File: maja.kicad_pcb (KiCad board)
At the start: 2 copper layers, 0 parts

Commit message: Started with basic PCB layout. Footprints must be checked again! I just choose one to be able to do a prelimary placement
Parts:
- added C1: 1uF, SMD_Packages:SM0603_Capa, F.Cu at (5.08, -5.08)
- added C10: 1uF, SMD_Packages:SM0603_Capa, F.Cu at (8.89, -6.35)
- added C11: 100nF, SMD_Packages:SM0603_Capa, F.Cu at (5.08, -2.54)
- added C12: 100nF, SMD_Packages:SM0603_Capa, F.Cu at (-8.89, -3.81)
- added C13: 1uF, SMD_Packages:SM0603_Capa, F.Cu at (1.27, -7.62)
- added C14: 100nF, SMD_Packages:SM0603_Capa, F.Cu at (-14.0, -1.27)
- added C15: 100nF, SMD_Packages:SM0603_Capa, F.Cu at (-10.2, -7.62)
- added C16: 100nF, SMD_Packages:SM0603_Capa, F.Cu at (-2.54, -5.08)
- added C17: 100nF, SMD_Packages:SM0603_Capa, F.Cu at (-8.89, -1.27)
- added C18: C, SMD_Packages:SM0603_Capa, F.Cu at (101.1, 99.8)
- added C19: C, SMD_Packages:SM0603_Capa, F.Cu at (90.2, 94.0)
- added C2: 1uF, SMD_Packages:SM0603_Capa, F.Cu at (6.35, 2.54)
- added C20: C, SMD_Packages:SM0603_Capa, F.Cu at (92.1, 94.0)
- added C21: 47p, SMD_Packages:SM0603_Capa, F.Cu at (0.00, -1.27)
- added C22: 1uF, SMD_Packages:SM0603_Capa, F.Cu at (119.4, 110.2)
- added C23: C, SMD_Packages:SM0603_Capa, F.Cu at (89.4, 90.9)
- added C24: C, SMD_Packages:SM0603_Capa, F.Cu at (91.9, 87.6)
- added C25: 2.2uF, SMD_Packages:SM0603_Capa, F.Cu at (108.7, 114.0)
- added C26: C, SMD_Packages:SM0603_Capa, F.Cu at (91.7, 80.5)
- added C27: C, SMD_Packages:SM0603_Capa, F.Cu at (83.8, 128.0)
- added C28: C, SMD_Packages:SM0603_Capa, F.Cu at (91.9, 140.2)
- added C3: 12pF, SMD_Packages:SM0603_Capa, F.Cu at (102.4, 87.9)
- added C31: 47p, SMD_Packages:SM0603_Capa, F.Cu at (8.89, -8.89)
- added C4: 22pF, SMD_Packages:SM0603_Capa, F.Cu at (72.9, 89.2)
- added C5: 1uF, SMD_Packages:SM0603_Capa, F.Cu at (2.54, -12.7)
- added C6: 1uF, SMD_Packages:SM0603_Capa, F.Cu at (10.2, -2.54)
- added C7: 12pF, SMD_Packages:SM0603_Capa, F.Cu at (112.3, 87.9)
- added C8: 22pF, SMD_Packages:SM0603_Capa, F.Cu at (72.9, 95.8)
- added C9: 1uF, SMD_Packages:SM0603_Capa, F.Cu at (5.08, -8.89)
- added D1: LED, LEDs:LED-0603, F.Cu at (93.0, 115.3)
- added D2: LED, LEDs:LED-0603, F.Cu at (95.2, 115.3)
- added J1: USB, Connect:USB_B, F.Cu at (114.9, 123.8)
- added K1: CONN_3, Pin_Headers:Pin_Header_Straight_1x03, F.Cu at (115.6, 99.6)
- added L1: INDUCTOR, SMD_Packages:SM0805, F.Cu at (93.0, 90.9)
- added L2: INDUCTOR, SMD_Packages:SM0805, F.Cu at (89.9, 87.6)
- added L3: INDUCTOR, SMD_Packages:SM0805, F.Cu at (90.9, 83.6)
- added L4: INDUCTOR, SMD_Packages:SM0805, F.Cu at (90.9, 77.2)
- added P1: JTAG, Pin_Headers:Pin_Header_Straight_2x05, F.Cu at (69.6, 121.4)
- added P2: CONN_8, Pin_Headers:Pin_Header_Straight_1x08, F.Cu at (61.7, 105.7)
- added R1: R, SMD_Packages:SM0603_Resistor, F.Cu at (93.0, 118.1)
- added R2: R, SMD_Packages:SM0603_Resistor, F.Cu at (95.2, 118.1)
- added R21: 33O, SMD_Packages:SM0603_Resistor, F.Cu at (104.9, 127.0)
- added R3: 56k, SMD_Packages:SM0603_Resistor, F.Cu at (84.1, 94.0)
- added R31: 33O, SMD_Packages:SM0603_Resistor, F.Cu at (104.9, 129.0)
- added R32: 1.5k, SMD_Packages:SM0603_Resistor, F.Cu at (105.9, 131.8)
- added R4: 2.2, SMD_Packages:SM0603_Resistor, F.Cu at (104.4, 99.1)
- added SW1: RESET, Discret:SW_PUSH_SMALL, F.Cu at (71.6, 141.7)
- added SW2: BTN, Discret:SW_PUSH_SMALL, F.Cu at (83.8, 123.4)
- added SW3: BTN, Discret:SW_PUSH_SMALL, F.Cu at (91.9, 135.6)
- added U1: CC2538, RTQ:RTQ, F.Cu at (92.1, 102.2)
- added U2: TPS70933, SMD_Packages:SOT223, F.Cu at (112.3, 109.0)
- added U3: Antenna, Oddities:NetTie-I_SMD, F.Cu at (90.9, 69.3)
- added X1: 32MHz, Crystals:Crystal_HC49-SD_SMD, F.Cu at (108.2, 91.9)
- added X2: 32kHz, Crystals:Crystal_Round_Horizontal_3mm_BigPad, F.Cu at (72.4, 92.7)
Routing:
- net Net-(C20-Pad1): track 0.00 -> 4.88 mm
- net Net-(C19-Pad1): track 0.00 -> 4.74 mm
- net Net-(C24-Pad2): track 0.00 -> 4.52 mm
- net Net-(C26-Pad1): track 0.00 -> 4.45 mm
- net /RF_P: track 0.00 -> 3.90 mm
- net /RF_N: track 0.00 -> 3.86 mm
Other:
- net class Default: clearance 0.254 -> 0.2; trace_width 0.254 -> 0.2
- rule trace_clearance: 0.254 -> 0.2
- rule trace_min: 0.254 -> 0.2

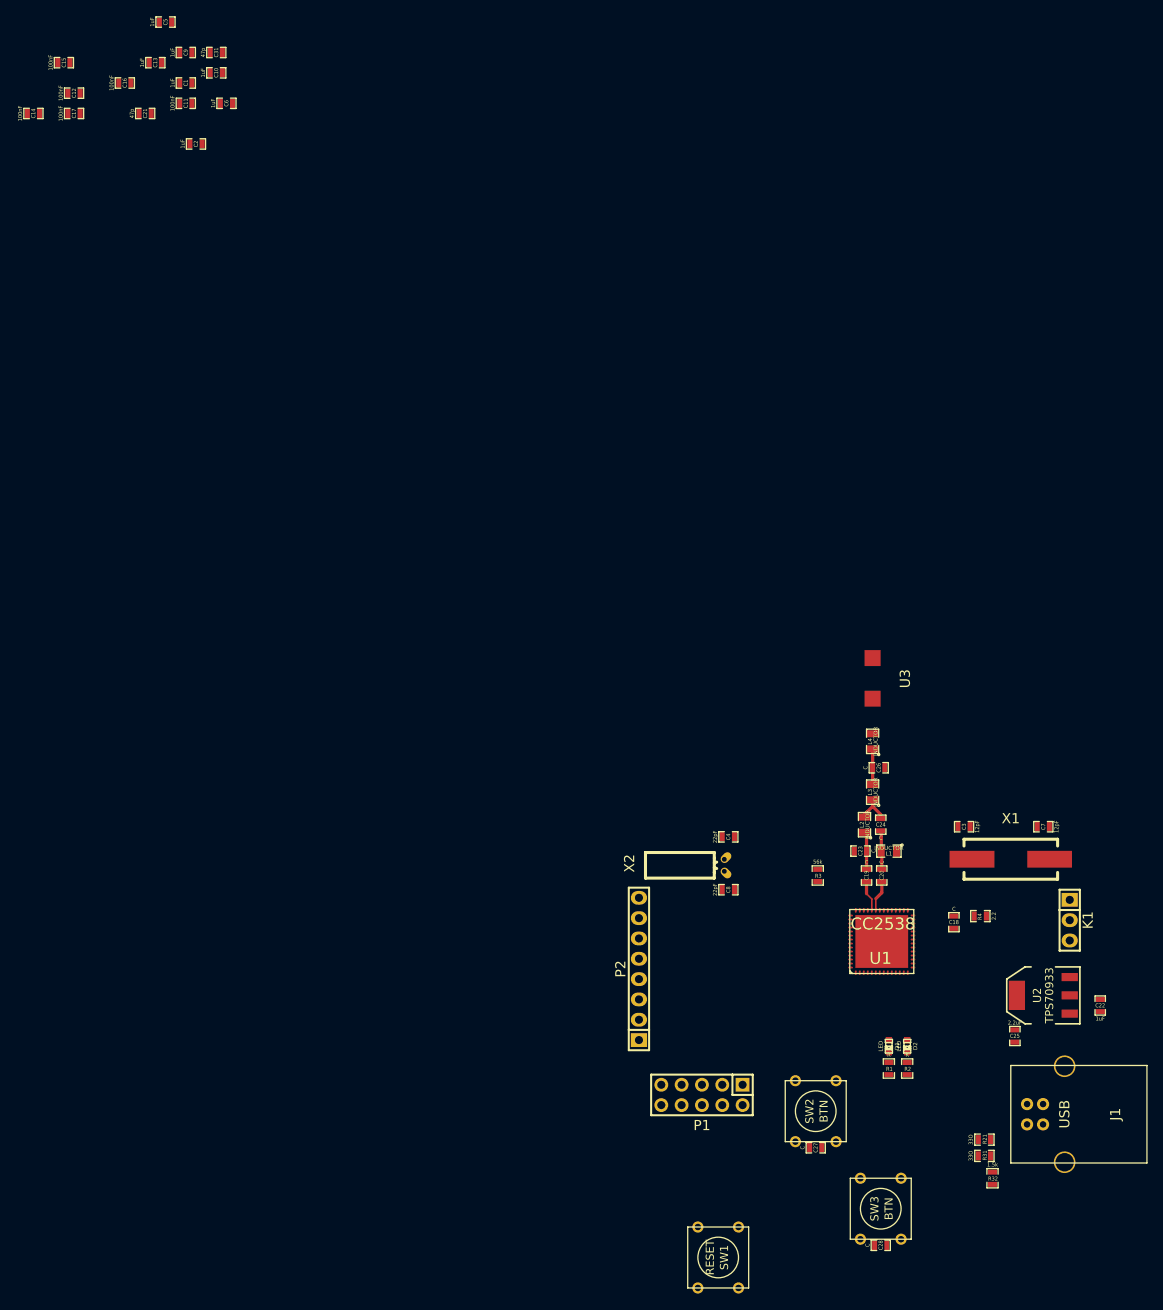
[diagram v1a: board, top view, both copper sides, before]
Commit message: Started with routing, added two missing JTAG signals and corrected one library error
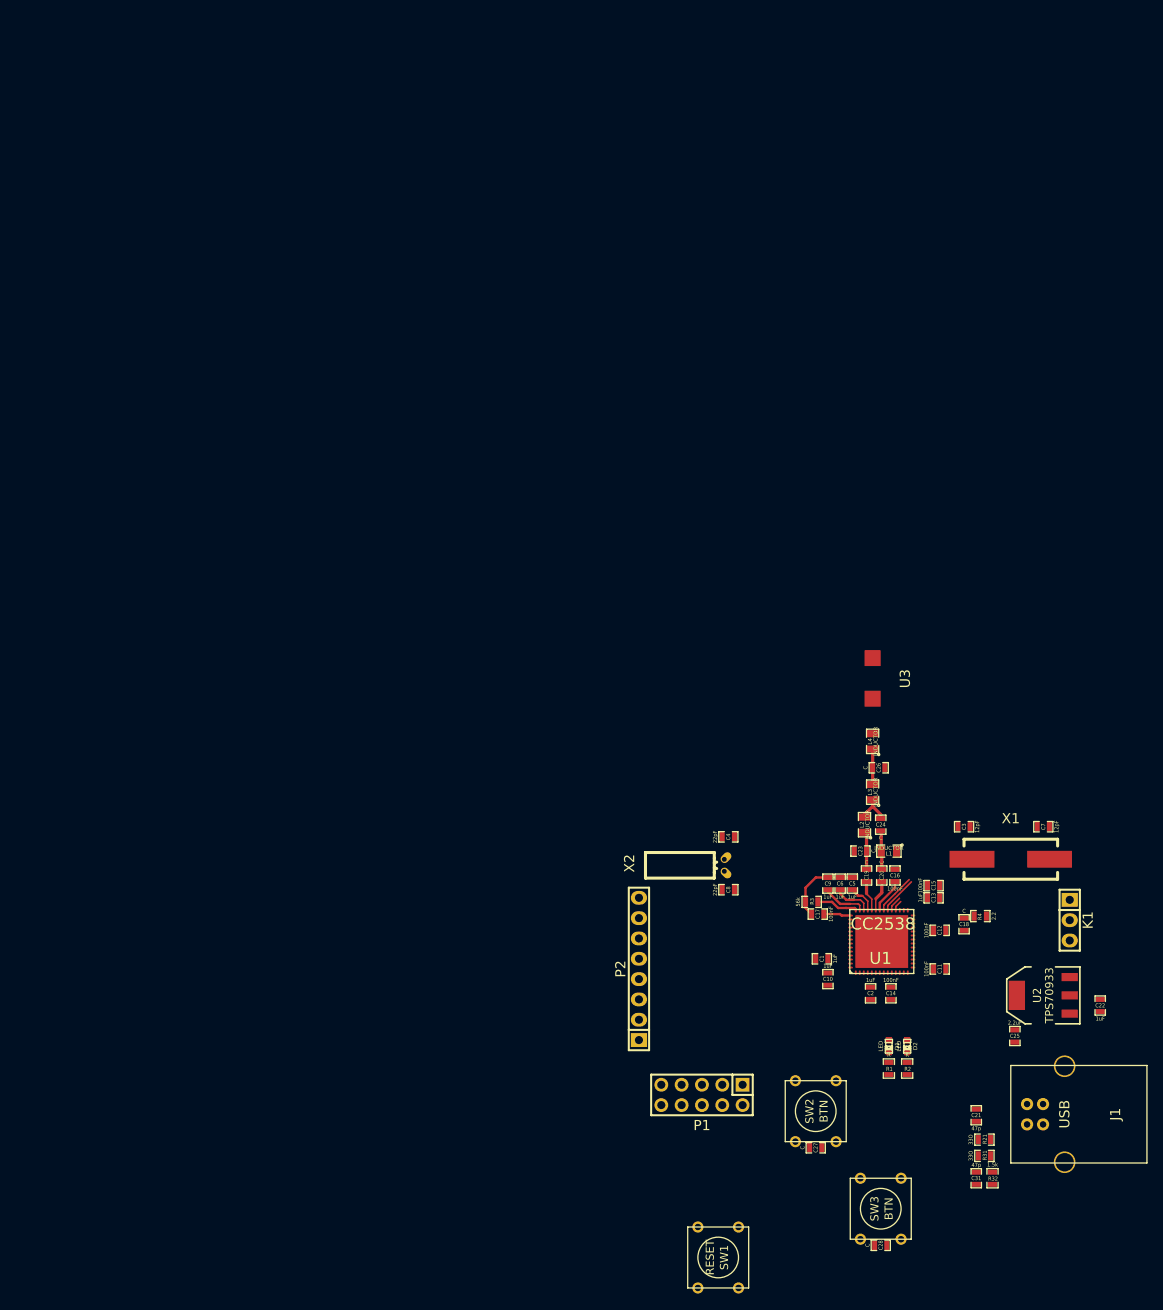
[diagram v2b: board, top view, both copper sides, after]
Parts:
- moved C31 169.8 mm to (103.9, 131.8), turned to 270 degrees
- moved C21 162.7 mm to (103.9, 124.0), turned to 90 degrees
- moved C14 153.6 mm to (93.2, 108.7), turned to 270 degrees
- moved C12 150.5 mm to (99.3, 100.8)
- moved C15 149.7 mm to (98.6, 95.2)
- moved C11 143.5 mm to (99.3, 105.7)
- moved C13 142.7 mm to (98.6, 96.8)
- moved C16 138.1 mm to (93.7, 94.0), turned to 90 degrees
- moved C5 137.7 mm to (88.4, 95.0), turned to 90 degrees
- moved C10 136.7 mm to (85.3, 106.9), turned to 270 degrees
- moved C17 136.6 mm to (84.1, 98.8), turned to 180 degrees
- moved C2 135.6 mm to (90.7, 108.7), turned to 270 degrees
- moved C1 135.3 mm to (84.6, 104.4), turned to 180 degrees
- moved C9 131.3 mm to (85.3, 95.0), turned to 90 degrees
- moved C6 124.1 mm to (86.9, 95.0), turned to 90 degrees
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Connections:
- U1 pad 22: Net-(U1-Pad22) -> Net-(P2-Pad1)
- U1 pad 23: Net-(U1-Pad23) -> Net-(P2-Pad2)
- U1 pad 35: (no net) -> Net-(C7-Pad1)
- U1 pad 48: Net-(P2-Pad8) -> /JTAG_TDO
- U1 pad 49: Net-(P2-Pad7) -> /JTAG_TDI
- U1 pad 5: Net-(P2-Pad1) -> Net-(P2-Pad3)
- U1 pad 50: Net-(P2-Pad6) -> Net-(P2-Pad8)
- U1 pad 51: Net-(P2-Pad5) -> Net-(P2-Pad7)
- U1 pad 52: Net-(P2-Pad4) -> Net-(P2-Pad5)
- U1 pad 53: Net-(P2-Pad3) -> Net-(P2-Pad5)
- U1 pad 54: Net-(P2-Pad2) -> Net-(P2-Pad4)
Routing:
- net VDD: track 0.00 -> 23.8 mm
- net GND: track 0.00 -> 9.99 mm
- net Net-(R3-Pad2): track 0.00 -> 5.29 mm
- net Net-(C7-Pad1): track 0.00 -> 5.16 mm
- net Net-(C3-Pad1): track 0.00 -> 4.79 mm
- net Net-(C10-Pad1): track 0.00 -> 1.35 mm
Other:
- net class Default: via_dia 0.889 -> 1.3; via_drill 0.635 -> 0.9

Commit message: Sync
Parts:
- C19, C20: value C -> 18pF
- C23, C24: value C -> 1pF
- C26: value C -> 1.2pF
- J1: footprint Connect:USB_B -> Connect:USB_MINI_B
- L1, L2, L3: value INDUCTOR -> 2nH
- L4: value INDUCTOR -> 3.3nH
- moved C7 14.0 mm to (98.8, 84.1)
- moved C25 9.43 mm to (99.6, 111.8), turned to 180 degrees
- moved C4 9.25 mm to (81.5, 92.5)
- moved X2 8.52 mm to (80.0, 88.9), turned to 0 degrees
- moved C22 6.86 mm to (112.5, 110.2)
- moved C8 6.27 mm to (78.2, 92.5), turned to 180 degrees
- moved U2 5.84 mm to (106.4, 109.0)
- moved C3 5.47 mm to (100.3, 93.0)
- moved X1 5.29 mm to (103.9, 88.9), turned to 90 degrees
- moved K1 4.34 mm to (111.5, 101.1)
- moved P2 4.33 mm to (65.0, 102.9)
- moved C18 2.51 mm to (100.6, 98.3), turned to 90 degrees
- moved P1 2.17 mm to (67.6, 120.7), turned to 90 degrees
- moved C11 1.63 mm to (98.0, 106.7), turned to 270 degrees
- moved L4 1.52 mm to (90.9, 78.7)
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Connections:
- C22 pad 2: Net-(C22-Pad2) -> GND
- U1 pad 52: Net-(P2-Pad5) -> Net-(P2-Pad6)
- U2 pad 2: Net-(C22-Pad2) -> GND
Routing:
- net GND: track 9.99 -> 117.7 mm
- net VDD: track 23.8 -> 113.5 mm, vias 0 -> 5
- net Net-(C8-Pad1): track 0.00 -> 19.9 mm
- net Net-(C4-Pad1): track 0.00 -> 18.3 mm
- net Net-(C7-Pad1): track 5.16 -> 23.4 mm
- net /BL_TX: track 0.00 -> 18.0 mm
- net /BL_RX: track 0.00 -> 17.3 mm
- net Net-(C3-Pad1): track 4.79 -> 18.5 mm
- net Net-(C18-Pad1): track 0.00 -> 6.67 mm
- net Net-(P2-Pad1): track 0.00 -> 6.52 mm, vias 0 -> 1
- net Net-(P2-Pad2): track 0.00 -> 5.45 mm, vias 0 -> 1
- net Net-(C10-Pad1): track 1.35 -> 4.63 mm
- net /V_USB: track 0.00 -> 2.90 mm
- net /nReset: track 0.00 -> 2.03 mm, vias 0 -> 1
- net Net-(C20-Pad1): track 4.88 -> 4.12 mm
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
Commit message: More layouting...
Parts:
- moved SW1 30.8 mm to (78.7, 111.8)
- moved C28 23.8 mm to (78.7, 120.4)
- moved SW3 18.3 mm to (78.7, 122.9)
- moved P1 15.8 mm to (51.8, 121.2)
- moved R32 14.9 mm to (100.8, 117.9), turned to 90 degrees
- moved C31 13.7 mm to (97.5, 119.6), turned to 90 degrees
- moved C27 12.0 mm to (90.7, 118.1)
- moved R31 9.89 mm to (100.1, 120.4)
- moved P2 9.72 mm to (68.3, 93.7)
- moved J1 7.57 mm to (108.0, 120.9), turned to 180 degrees
- moved SW2 6.90 mm to (90.7, 122.7)
- moved R21 6.82 mm to (100.1, 122.2)
- moved C21 6.43 mm to (97.5, 122.9), turned to 270 degrees
- moved D1 3.78 mm to (94.2, 111.8)
- moved D2 3.64 mm to (96.0, 111.8)
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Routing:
- net GND: track 117.7 -> 213.7 mm
- net /Btn1: track 0.00 -> 31.6 mm
- net /V_USB: track 2.90 -> 30.1 mm, vias 0 -> 2
- net /Btn0: track 0.00 -> 15.3 mm
- net /USB_FS_PULLUP: track 0.00 -> 13.2 mm
- net VDD: track 113.5 -> 123.4 mm, vias 5 -> 6
- net Net-(J1-Pad3): track 0.00 -> 5.65 mm
- net /STATUS_LED: track 0.00 -> 5.37 mm
- net /USB_P: track 0.00 -> 5.16 mm, vias 0 -> 1
- net /USB_N: track 0.00 -> 4.59 mm, vias 0 -> 1
- net Net-(J1-Pad2): track 0.00 -> 3.86 mm
- net Net-(C10-Pad1): track 4.63 -> 7.83 mm
- net Net-(D2-Pad2): track 0.00 -> 1.54 mm
- net Net-(D1-Pad2): track 0.00 -> 1.54 mm

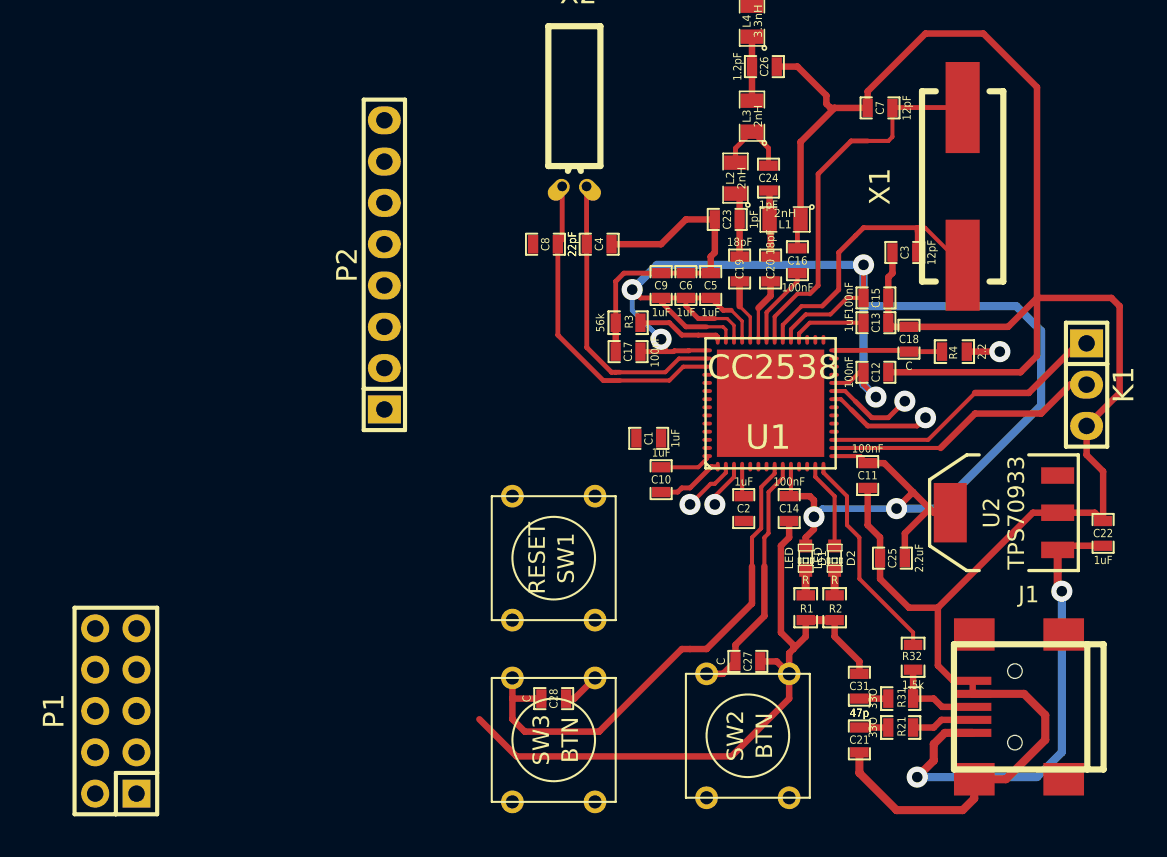
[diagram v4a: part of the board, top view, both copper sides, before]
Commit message: Finished routing more or less, it is a real pain and uses much too much vias. We have to optimize this if possible
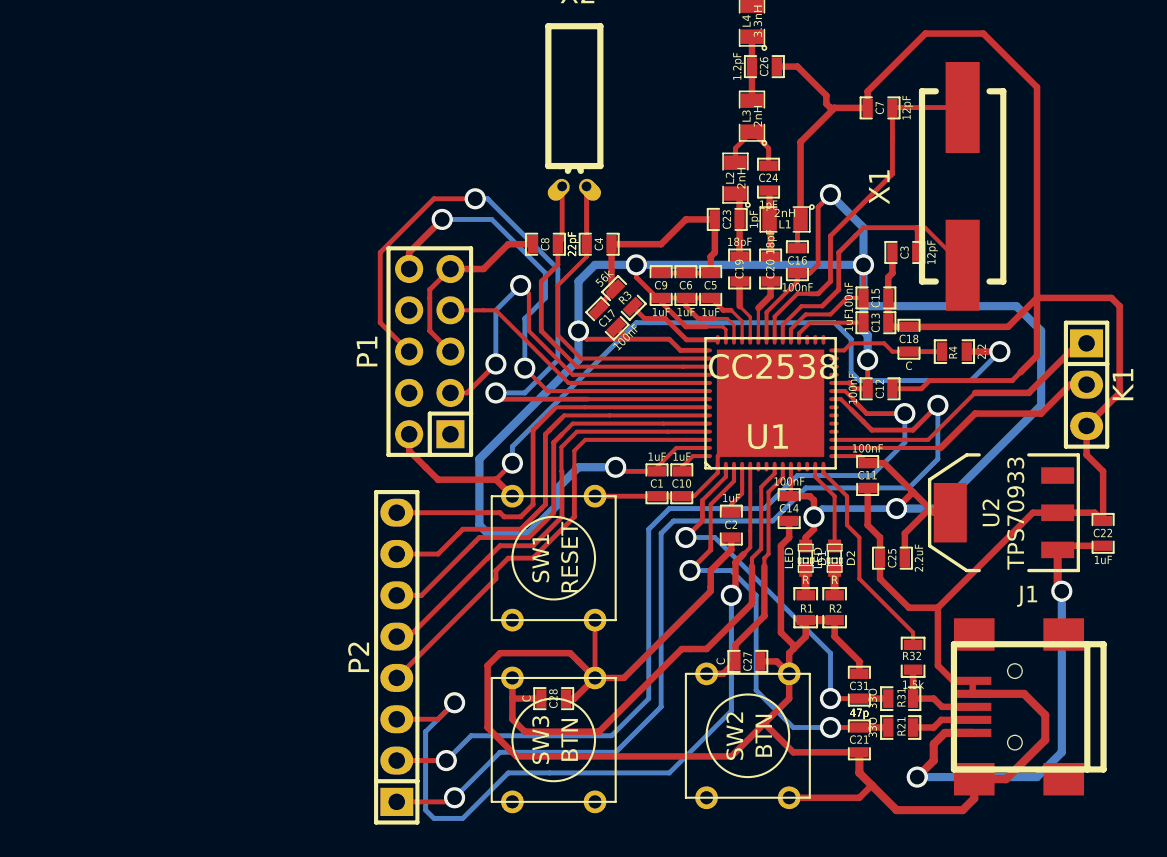
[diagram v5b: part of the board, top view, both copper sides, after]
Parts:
- moved P1 29.3 mm to (71.1, 99.1)
- moved P2 24.1 mm to (69.1, 117.9)
- moved C1 2.84 mm to (85.1, 107.2), turned to 270 degrees
- moved C17 2.40 mm to (82.0, 97.0), turned to 135 degrees
- moved R3 1.55 mm to (83.1, 95.8), turned to 315 degrees
- moved C10 1.30 mm to (86.6, 107.2)
- moved C2 1.27 mm to (89.7, 109.7)
- moved C12 1.05 mm to (98.8, 101.3)
- turned SW1 to 90 degrees
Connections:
- C13 pad 1: Net-(C10-Pad1) -> Net-(C13-Pad1)
- U1 pad 32: Net-(C10-Pad1) -> Net-(C13-Pad1)
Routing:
- net GND: track 213.7 -> 271.9 mm
- net Net-(P2-Pad1): track 6.52 -> 59.4 mm, vias 1 -> 2
- net VDD: track 123.4 -> 173.7 mm, vias 6 -> 8
- net Net-(P2-Pad3): track 0.00 -> 48.6 mm, vias 0 -> 2
- net /nReset: track 2.03 -> 49.5 mm, vias 1 -> 2
- net Net-(P2-Pad2): track 5.45 -> 52.2 mm, vias 1 -> 2
- net /JTAG_TDI: track 0.00 -> 44.9 mm, vias 0 -> 2
- net /JTAG_TDO: track 0.00 -> 29.8 mm, vias 0 -> 2
- net Net-(P2-Pad4): track 0.00 -> 27.8 mm
- net Net-(P2-Pad5): track 0.00 -> 26.9 mm
- net Net-(P2-Pad6): track 0.00 -> 26.0 mm
- net Net-(P2-Pad7): track 0.00 -> 25.1 mm
- net Net-(P2-Pad8): track 0.00 -> 24.7 mm
- net /JTAG_TMS: track 0.00 -> 24.1 mm, vias 0 -> 2
- net /USB_N: track 4.59 -> 27.1 mm, vias 1 -> 2
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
